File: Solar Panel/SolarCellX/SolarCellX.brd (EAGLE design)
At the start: 100 x 80 mm, 55 parts

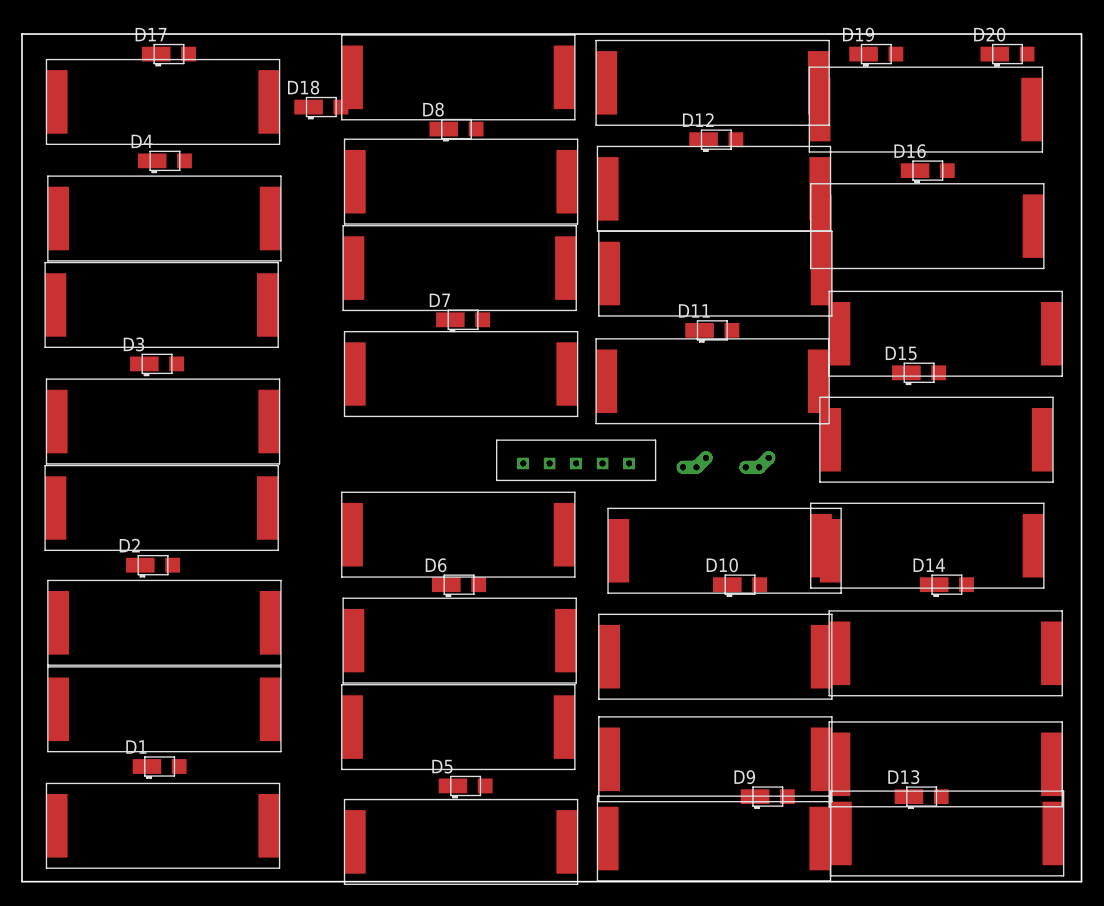
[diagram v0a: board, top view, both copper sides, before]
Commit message: Updated Solar Panel with Alex's new sizes
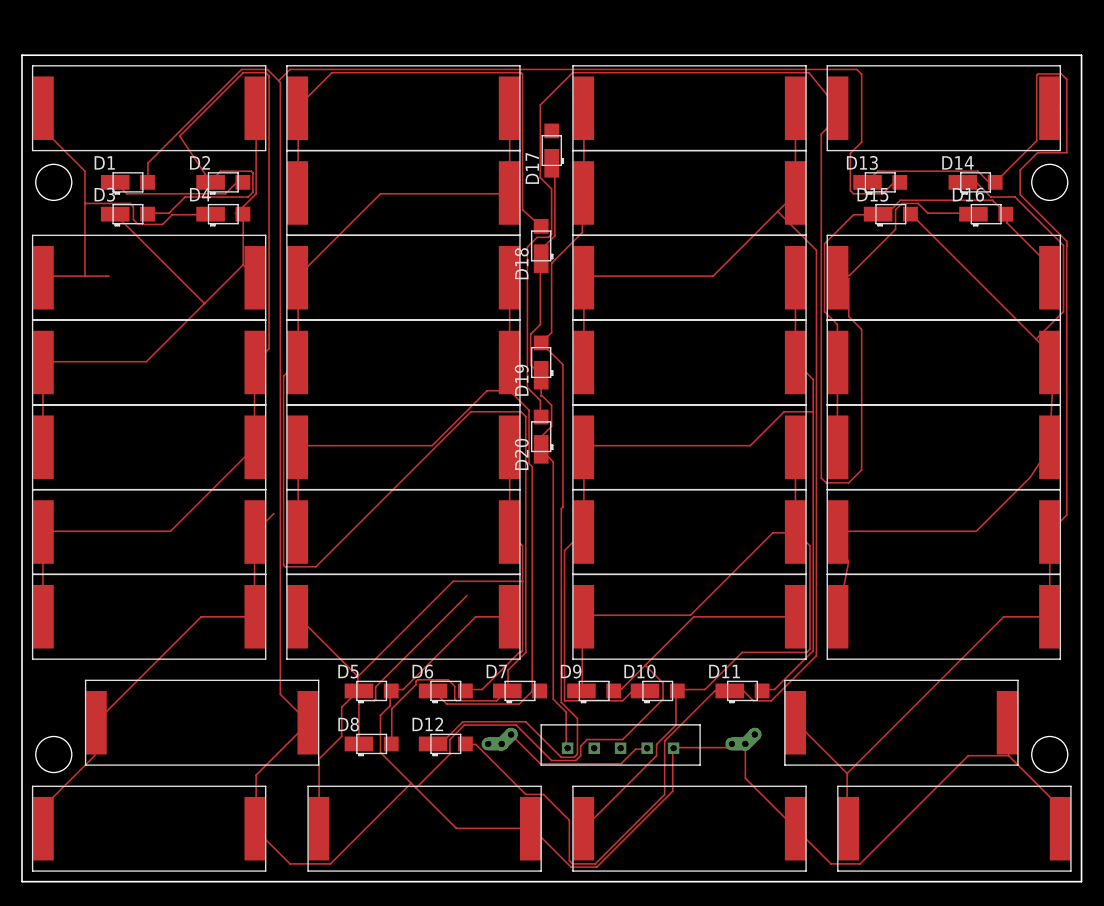
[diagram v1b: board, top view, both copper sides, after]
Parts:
- removed SLR11, SLR12, SLR13, SLR14, SLR15, SLR16, SLR17, SLR18, U$10, U$11, U$12, U$13, U$14, U$15, U$16, U$17, U$18, U$19, U$20, U$21, U$22, U$23, U$24, U$25, U$26, U$27, U$28, U$29, U$30, U$31, U$32, U$9: KXOB22-04X3F, Solar:KXOB22-04X3F
- added 11, 12, 13, 14, 15, 16, 17, 18, 21, 22, 23, 24, 25, 26, 27, 28, 31, 32, 33, 34, 35, 36, 37, 38, 41, 42, 43, 44, 45, 46, 47, 48: KXOB22-04X3F, Solar:KXOB22-04X3F
- moved D12 62.5 mm to (40.0, 13.0)
- moved D8 58.6 mm to (33.0, 13.0)
- moved D13 58.1 mm to (81.0, 66.0)
- moved D20 56.9 mm to (49.0, 42.0), turned to 90 degrees
- moved D1 55.2 mm to (10.0, 66.0)
- moved D19 43.0 mm to (49.0, 49.0), turned to 90 degrees
- moved D14 38.1 mm to (90.0, 66.0)
- moved D17 37.3 mm to (50.0, 69.0), turned to 90 degrees
- moved D2 36.7 mm to (19.0, 66.0)
- moved D7 35.4 mm to (47.0, 18.0)
- moved D11 34.1 mm to (68.0, 18.0)
- moved U$34 31.9 mm to (44.0, 13.0)
- moved U$33 27.2 mm to (49.0, 11.0)
- moved U$35 26.1 mm to (67.0, 13.0)
- moved D18 24.5 mm to (49.0, 60.0), turned to 90 degrees
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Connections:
- removed net N$11: D6.POS, U$11.P$2, U$12.P$2
- removed net N$12: D6.NEG, U$11.P$1, U$12.P$1
- removed net N$13: D7.POS, U$13.P$2, U$14.P$2
- removed net N$15: D8.POS, U$15.P$2, U$16.P$2
- removed net N$19: D10.POS, U$19.P$2, U$20.P$2
- removed net N$21: D11.POS, U$21.P$2, U$22.P$2
- removed net N$23: D12.POS, U$23.P$2, U$24.P$2
- removed net N$27: D14.POS, U$27.P$2, U$28.P$2
- removed net N$29: D15.POS, U$29.P$2, U$30.P$2
- removed net N$3: D2.POS, SLR13.P$2, SLR14.P$2
- removed net N$31: D16.POS, U$31.P$2, U$32.P$2
- removed net N$5: D3.POS, SLR15.P$2, SLR16.P$2
- removed net N$7: D4.POS, SLR17.P$2, SLR18.P$2
- new net N$9: 23.P$1, 24.P$1, 25.P$2, 26.P$2, D6.NEG, D7.POS
- net GND: now also 11.P$2, 12.P$2, 21.P$2, 22.P$2, 31.P$2, 32.P$2, 41.P$2, 42.P$2; no longer SLR11.P$2, SLR12.P$2, U$10.P$2, U$17.P$2, U$18.P$2, U$25.P$2, U$26.P$2, U$9.P$2
- net N$10: now also 21.P$1, 22.P$1, 23.P$2, 24.P$2, D6.POS; no longer U$10.P$1, U$9.P$1
- net N$14: now also 25.P$1, 26.P$1, 27.P$2, 28.P$2, D8.POS; no longer U$13.P$1, U$14.P$1
- net N$16: now also 27.P$1, 28.P$1; no longer U$15.P$1, U$16.P$1
- net N$18: now also 31.P$1, 32.P$1, 33.P$2, 34.P$2, D10.POS; no longer U$17.P$1, U$18.P$1
- net N$2: now also 11.P$1, 12.P$1, 13.P$2, 14.P$2, D2.POS; no longer SLR11.P$1, SLR12.P$1
- net N$20: now also 33.P$1, 34.P$1, 35.P$2, 36.P$2, D11.POS; no longer U$19.P$1, U$20.P$1
- net N$22: now also 35.P$1, 36.P$1, 37.P$2, 38.P$2, D12.POS; no longer U$21.P$1, U$22.P$1
- net N$24: now also 37.P$1, 38.P$1; no longer U$23.P$1, U$24.P$1
- net N$26: now also 41.P$1, 42.P$1, 43.P$2, 44.P$2, D14.POS; no longer U$25.P$1, U$26.P$1
- net N$28: now also 43.P$1, 44.P$1, 45.P$2, 46.P$2, D15.POS; no longer U$27.P$1, U$28.P$1
- net N$30: now also 45.P$1, 46.P$1, 47.P$2, 48.P$2, D16.POS; no longer U$29.P$1, U$30.P$1
- net N$32: now also 47.P$1, 48.P$1; no longer U$31.P$1, U$32.P$1
- net N$4: now also 13.P$1, 14.P$1, 15.P$2, 16.P$2, D3.POS; no longer SLR13.P$1, SLR14.P$1
- net N$6: now also 15.P$1, 16.P$1, 17.P$2, 18.P$2, D4.POS; no longer SLR15.P$1, SLR16.P$1
- net N$8: now also 17.P$1, 18.P$1; no longer SLR17.P$1, SLR18.P$1
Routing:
- net GND: track 0.00 -> 354.2 mm
- net N$32: track 0.00 -> 141.4 mm
- net N$22: track 0.00 -> 134.8 mm
- net N$14: track 0.00 -> 132.4 mm
- net N$26: track 0.00 -> 121.9 mm
- net N$4: track 0.00 -> 100.4 mm
- net N$20: track 0.00 -> 98.2 mm
- net N$9: track 0.00 -> 84.7 mm
- net N$28: track 0.00 -> 82.3 mm
- net N$24: track 0.00 -> 81.2 mm
- net N$18: track 0.00 -> 81.1 mm
- net N$10: track 0.00 -> 70.1 mm
- net N$16: track 0.00 -> 64.9 mm
- net N$6: track 0.00 -> 62.7 mm
- net V_SOLAR: track 0.00 -> 58.9 mm
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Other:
- board size 100 x 80 mm -> 100 x 78 mm
